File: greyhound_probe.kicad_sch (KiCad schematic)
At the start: 21 parts

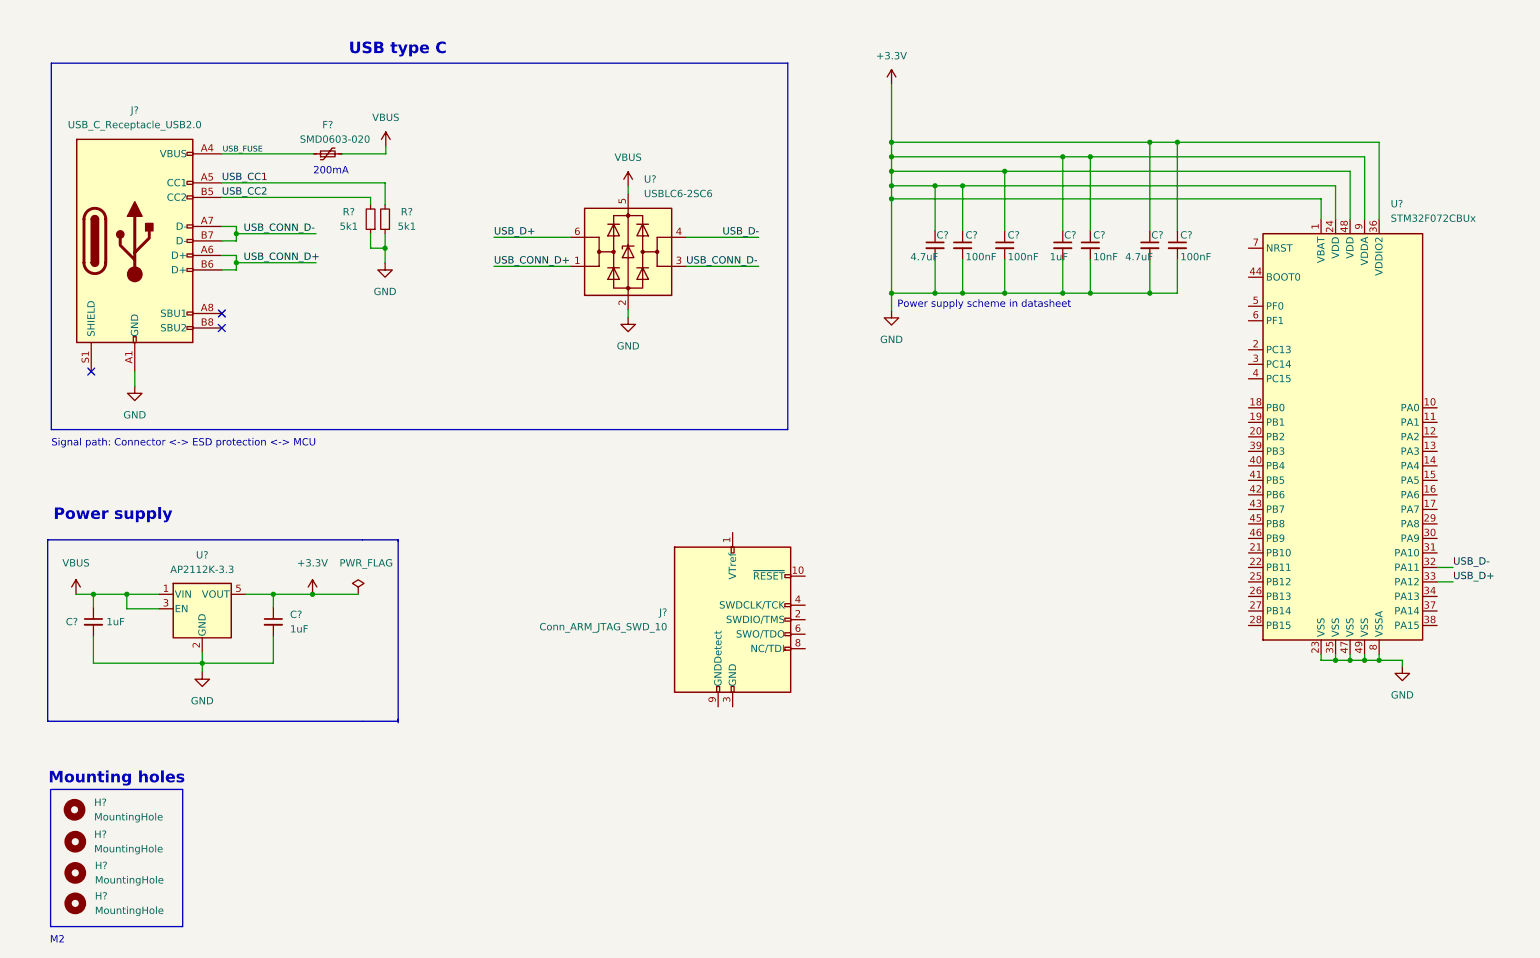
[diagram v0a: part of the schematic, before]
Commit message: Power supply rework, jtag connector finished
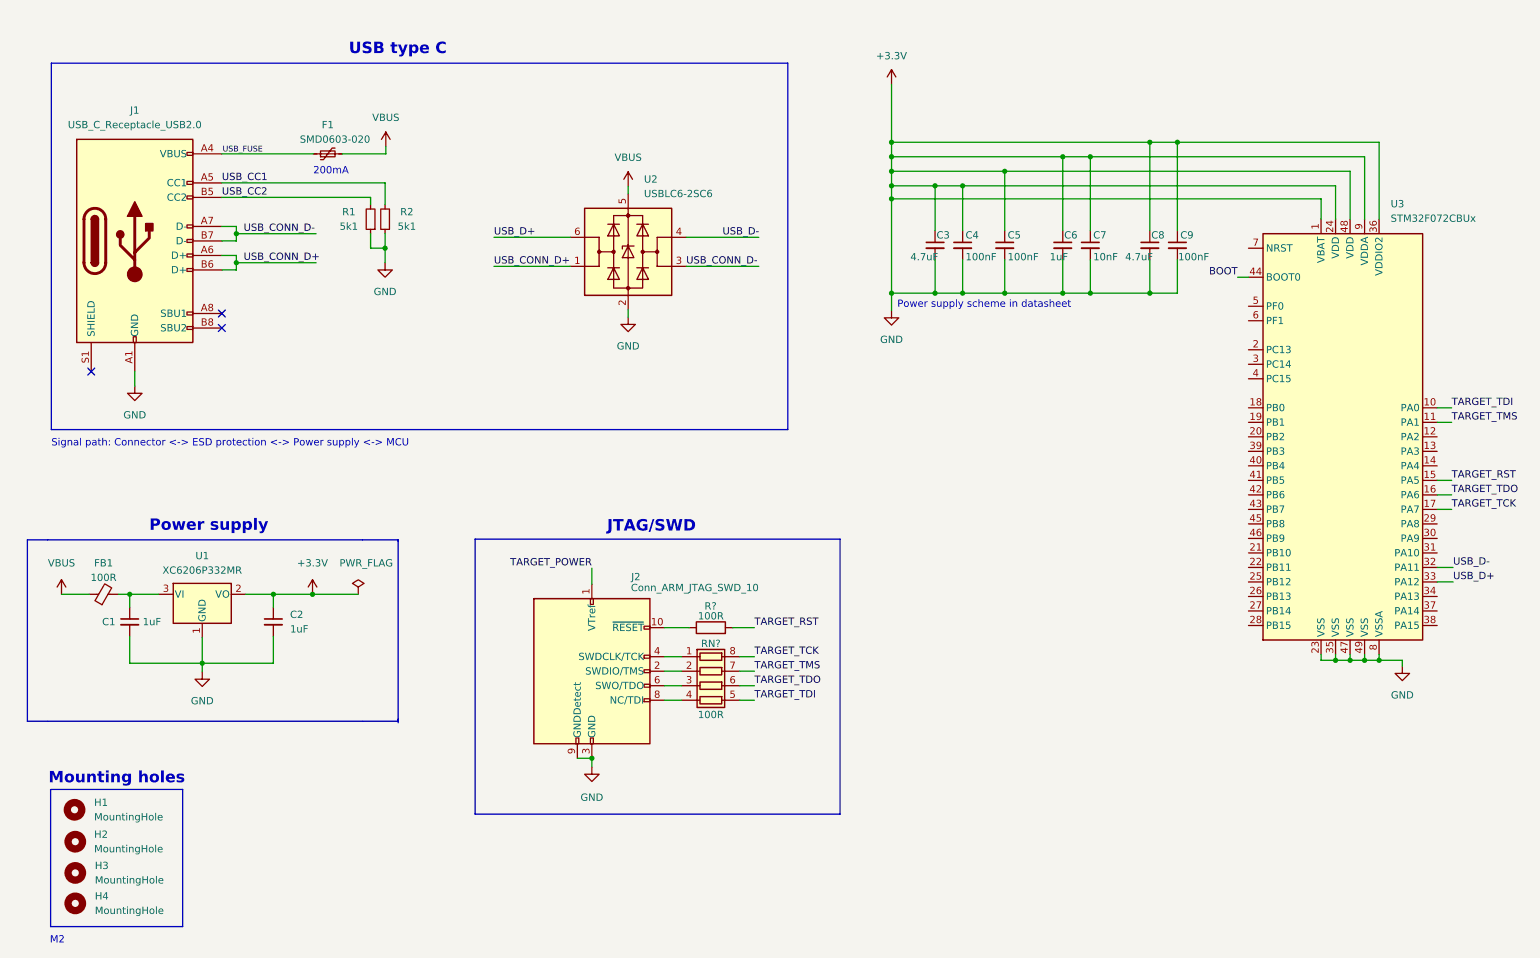
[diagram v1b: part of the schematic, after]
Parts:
- removed U?: AP2112K-3.3, Package_TO_SOT_SMD:SOT-23-5, symbol Regulator_Linear:AP2112K-3.3
- added FB1: 100R, Inductor_SMD:L_0603_1608Metric, symbol Device:FerriteBead_Small
- added R?: 100R, Resistor_SMD:R_0603_1608Metric, symbol Device:R
- added RN?: 100R, Resistor_SMD:R_Array_Convex_4x0603, symbol Device:R_Pack04
- added U1: XC6206P332MR, Package_TO_SOT_SMD:SOT-23, symbol Regulator_Linear:XC6206PxxxMR
- C1, C2, C3, C4, C5, C6, C7, C8, C9: renamed from C?; footprint (none) -> Capacitor_SMD:C_0603_1608Metric
- gave numbers to parts that had none: 11
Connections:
- net +3.3V: now also J2.3 (GND), J2.5 (GND), J2.9 (GNDDetect), U1.1 (GND), U1.2 (VO)
- net VBUS: now also FB1.1; no longer C1.1
- net TARGET_POWER: now reaches J2.1 (VTref)
- net at J2.10 (~{RESET}): now also R?.1
- net at J2.2 (SWDIO/TMS): now also RN?.2 (R2.1)
- net at J2.4 (SWDCLK/TCK): now also RN?.1 (R1.1)
- net at J2.6 (SWO/TDO): now also RN?.3 (R3.1)
- net at J2.8 (NC/TDI): now also RN?.4 (R4.1)
- net TARGET_TDI: now reaches U3.10 (PA0)
- net TARGET_TDI: now also RN?.5 (R4.2)
- net TARGET_TMS: now reaches U3.11 (PA1)
- net TARGET_TMS: now also RN?.7 (R2.2)
- net TARGET_RST: now reaches U3.15 (PA5)
- net TARGET_RST: now also R?.2
- net TARGET_TDO: now reaches U3.16 (PA6)
- net TARGET_TDO: now also RN?.6 (R3.2)
- net TARGET_TCK: now reaches U3.17 (PA7)
- net TARGET_TCK: now also RN?.8 (R1.2)
- net BOOT: now reaches U3.44 (BOOT0)
- new net: C1.1, FB1.2, U1.3 (VI)
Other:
- note added: "JTAG/SWD"
- note added: "Signal path: Connector <-> ESD protection <-> Power supply <-> MCU"
- note removed: "Signal path: Connector <-> ESD protection <-> MCU"
- moved on the sheet: C1, J2

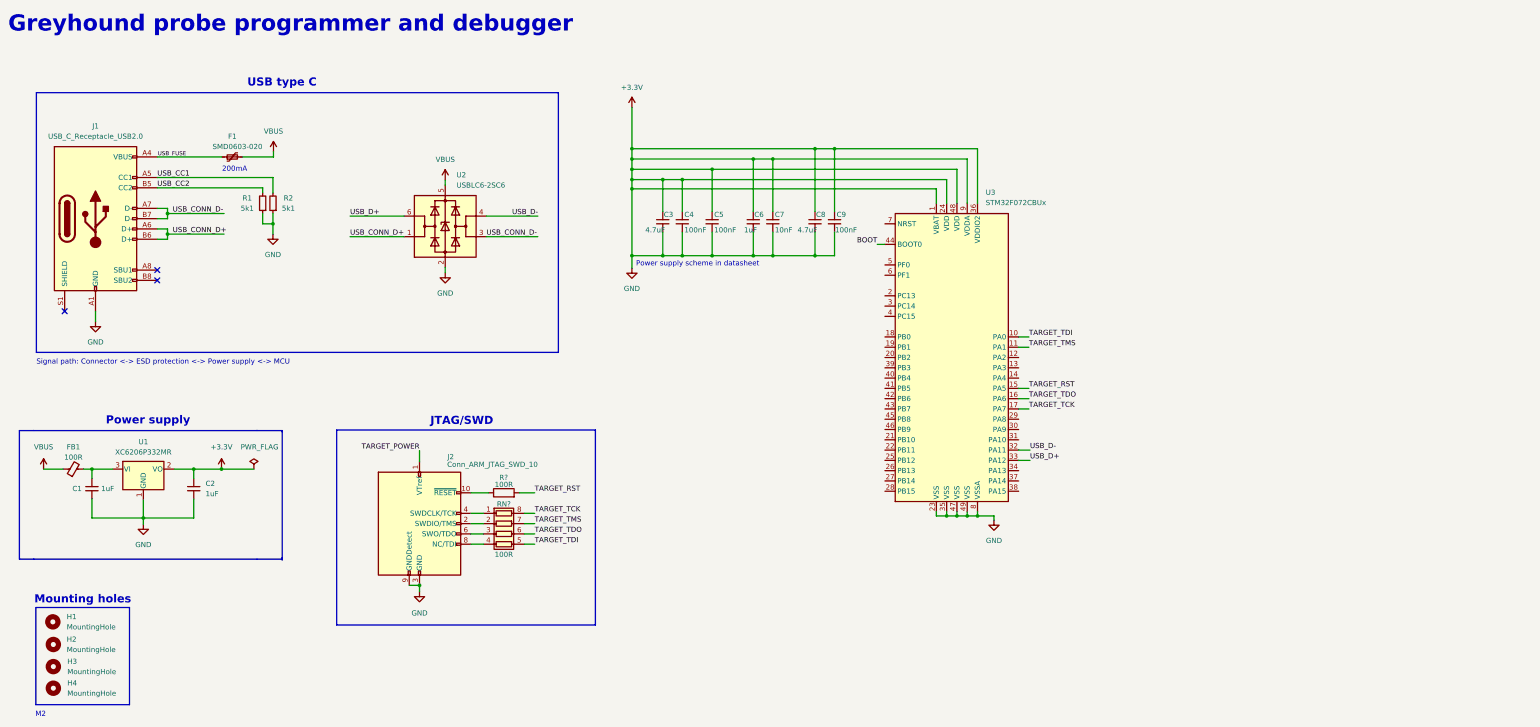
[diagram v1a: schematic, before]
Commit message: Led resistors changed, boot button
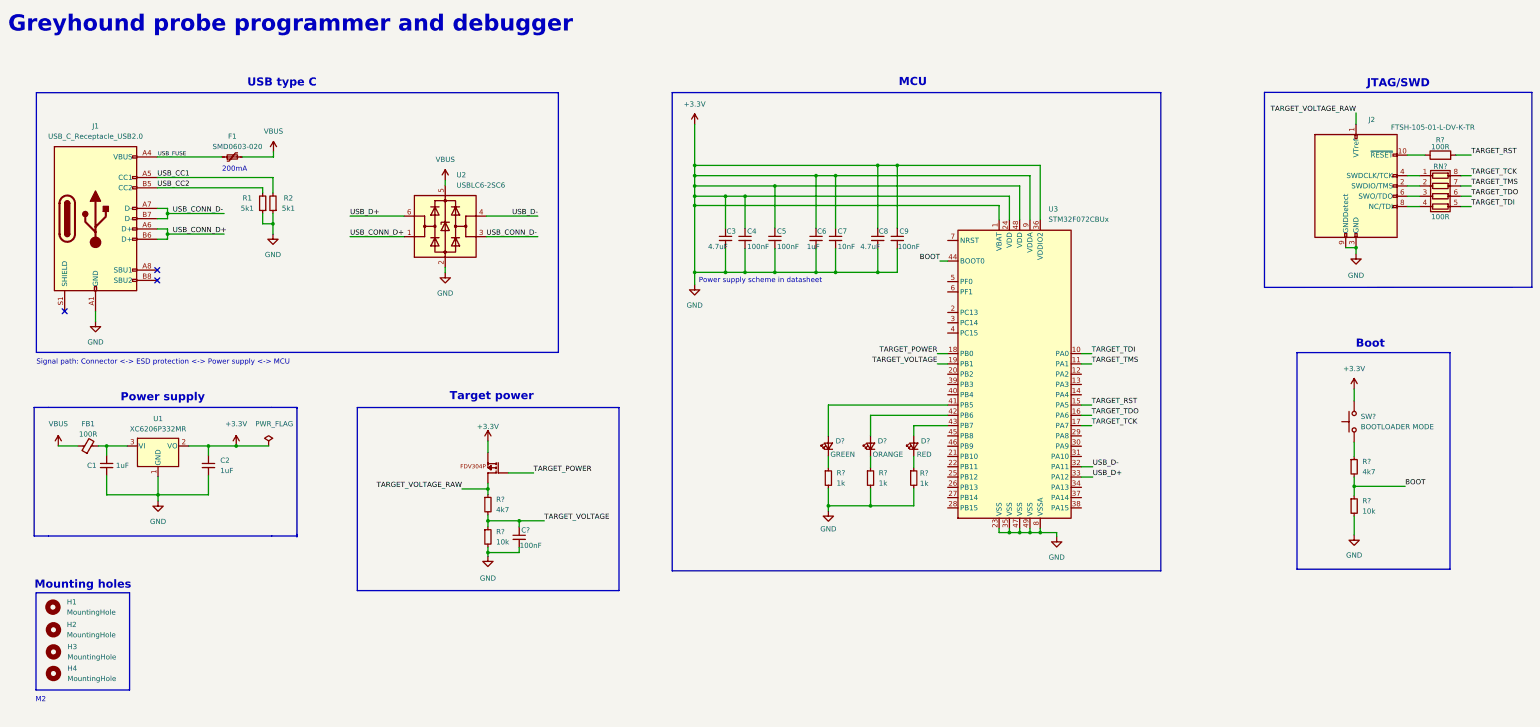
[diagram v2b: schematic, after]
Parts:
- added C?: 100nF, Capacitor_SMD:C_0603_1608Metric, symbol Device:C_Small
- added D?: RED, Diode_SMD:D_0603_1608Metric, symbol Device:LED_Small
- added D?: ORANGE, Diode_SMD:D_0603_1608Metric, symbol Device:LED_Small
- added D?: GREEN, Diode_SMD:D_0603_1608Metric, symbol Device:LED_Small
- added R? (x3): 1k, Resistor_SMD:R_0603_1608Metric, symbol Device:R_Small
- added R? (x2): 10k, Resistor_SMD:R_0603_1608Metric, symbol Device:R_Small
- added R? (x2): 4k7, Resistor_SMD:R_0603_1608Metric, symbol Device:R_Small
- added SW?: BOOTLOADER MODE, symbol Switch:SW_Push
- added U?: FDV304P, SOT23-3, symbol greyhound_library:FDV304P
- J2: value Conn_ARM_JTAG_SWD_10 -> FTSH-105-01-L-DV-K-TR; LCSC Part (none) -> C448647
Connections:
- net +3.3V: now also C?.2, R?.2, R?.2, R?.2, R?.2, R?.2, SW?.2, U?.2
- net BOOT: now also R?.1, R?.2
- net TARGET_POWER: now also U3.18 (PB0), U?.1; no longer J2.1 (VTref)
- net TARGET_VOLTAGE: now reaches U3.19 (PB1)
- net TARGET_VOLTAGE: now also C?.1, R?.1, R?.2
- net at U3.41 (PB5): now also D?.2 (A)
- net at U3.42 (PB6): now also D?.2 (A)
- net at U3.43 (PB7): now also D?.2 (A)
- new net: D?.1 (K), R?.1 (x3)
- new net: R?.1, SW?.1
- new net TARGET_VOLTAGE_RAW: J2.1 (VTref), R?.1, U?.3
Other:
- note added: "Boot"
- note added: "MCU"
- note added: "Target power"
- moved on the sheet: C1, C2, C3, C4, C5, C6, C7, C8, C9, FB1, H1, H2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

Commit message: Added UART, started with PCB sectioning
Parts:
- removed R?: 10k, Resistor_SMD:R_0603_1608Metric, symbol Device:R_Small
- removed R?: 4k7, Resistor_SMD:R_0603_1608Metric, symbol Device:R_Small
- removed SW?: BOOTLOADER MODE, symbol Switch:SW_Push
- removed U?: FDV304P, SOT23-3, symbol greyhound_library:FDV304P
- added C11: 100nF, Capacitor_SMD:C_0603_1608Metric, symbol Device:C_Small
- added J2: Conn_01x04_Male, Connector_PinHeader_2.54mm:PinHeader_1x04_P2.54mm_Vertical, symbol Connector:Conn_01x04_Male
- added Q1: IRLML6401, Package_TO_SOT_SMD:SOT-23, symbol Transistor_FET:IRLML6401
- added R10, R9: 100R, Resistor_SMD:R_0603_1608Metric, symbol Device:R
- added R8: 10k, Resistor_SMD:R_0603_1608Metric, symbol Device:R
- added SW1: SW_SPDT, Button_Switch_SMD:SW_SPDT_PCM12, symbol Switch:SW_SPDT
- gave numbers to parts that had none: 11
- renumbered C9 to C10, C3 to C4, C4 to C5, C5 to C6, C6 to C7, C7 to C8, C8 to C9, J2 to J3
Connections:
- net +3.3V: now also D1.1 (K), D2.1 (K), D3.1 (K), C11.2, J2.1 (Pin_1), J2.4 (Pin_4), Q1.2 (S), SW1.1 (A), SW1.3 (C); no longer R5.2, R6.2, R7.2
- net BOOT: now also R8.2
- net TARGET_POWER: now also Q1.1 (G)
- net TARGET_RST: now also U3.29 (PA8); no longer U3.15 (PA5)
- net TARGET_TCK: now also U3.26 (PB13); no longer U3.17 (PA7)
- net TARGET_TDI: now also U3.28 (PB15); no longer U3.10 (PA0)
- net TARGET_TDO: now also U3.25 (PB12); no longer U3.16 (PA6)
- net TARGET_TMS: now also U3.27 (PB14); no longer U3.11 (PA1)
- net TARGET_VOLTAGE_RAW: now also Q1.3 (D)
- net at R7.1: now also U3.43 (PB7); no longer D3.1 (K)
- net at D3.2 (A): now also R7.2; no longer U3.43 (PB7)
- net UART_TX: now reaches U3.21 (PB10)
- net UART_TX: now also R9.2
- net UART_RX: now reaches U3.22 (PB11)
- net UART_RX: now also R10.2
- net at U3.41 (PB5): now also R5.1; no longer D1.2 (A)
- net at U3.42 (PB6): now also R6.1; no longer D2.2 (A)
- net NRST: now reaches U3.7 (NRST)
- net NRST: now also C11.1
- new net: J2.2 (Pin_2), R9.1
- new net: J2.3 (Pin_3), R10.1
- new net: R8.1, SW1.2 (B)
- new net: D2.2 (A), R6.2
- new net: D1.2 (A), R5.2
- no-connect marks 3 -> 26
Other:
- note added: "0 - Run mode 1 - Boot into bootloader"
- note added: "Reset"
- note added: "UART"
- moved on the sheet: D1, D2, D3, R5, R6, R7

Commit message: Fixed short and power symbols
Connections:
- net +3.3V: no longer C1.2, C10.2, C11.2, C2.2, C3.2, C4.2, C5.2, C6.2, C7.2, C8.2, C9.2, D1.1 (K), D2.1 (K), D3.1 (K), J1.A1 (GND), J1.A12 (GND), J1.B1 (GND), J1.B12 (GND), J2.4 (Pin_4), J3.3 (GND), J3.5 (GND), J3.9 (GNDDetect), R1.1, R2.1, R4.2, SW1.1 (A), U1.1 (GND), U2.2 (GND), U3.23 (VSS), U3.35 (VSS), U3.47 (VSS), U3.49 (VSS), U3.8 (VSSA)
- net TARGET_TCK: now also U3.25 (PB12); no longer U3.26 (PB13)
- net TARGET_TDO: now also U3.27 (PB14); no longer U3.25 (PB12)
- net TARGET_TMS: now also U3.26 (PB13); no longer U3.27 (PB14)
- new net GND: C1.2, C10.2, C11.2, C2.2, C3.2, C4.2, C5.2, C6.2, C7.2, C8.2, C9.2, D1.1 (K), D2.1 (K), D3.1 (K), J1.A1 (GND), J1.A12 (GND), J1.B1 (GND), J1.B12 (GND), J2.4 (Pin_4), J3.3 (GND), J3.5 (GND), J3.9 (GNDDetect), R1.1, R2.1, R4.2, SW1.1 (A), U1.1 (GND), U2.2 (GND), U3.23 (VSS), U3.35 (VSS), U3.47 (VSS), U3.49 (VSS), U3.8 (VSSA)
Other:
- note added: "UART and JTAG/SWD are connected to 5V tolerant pins for better compatibility. SWD of MCU is not broken out because the factory default bootloader will be used."
